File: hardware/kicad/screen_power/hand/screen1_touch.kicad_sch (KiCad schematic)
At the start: 7 parts, among them J101 PI USB / XH4, J102 TOUCH / XH4, K101 IM02TS, Q101 2N7000

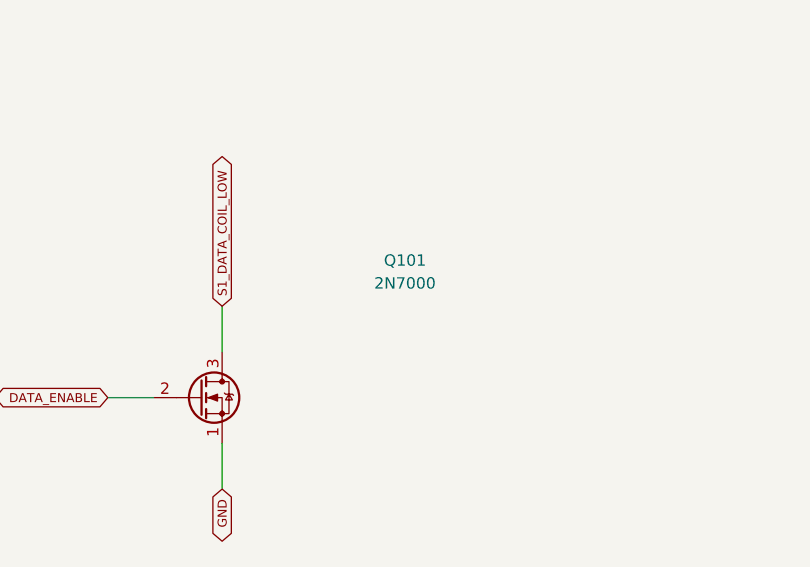
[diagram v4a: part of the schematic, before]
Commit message: fix(hardware): strengthen screen gate drive and finish PCB copper
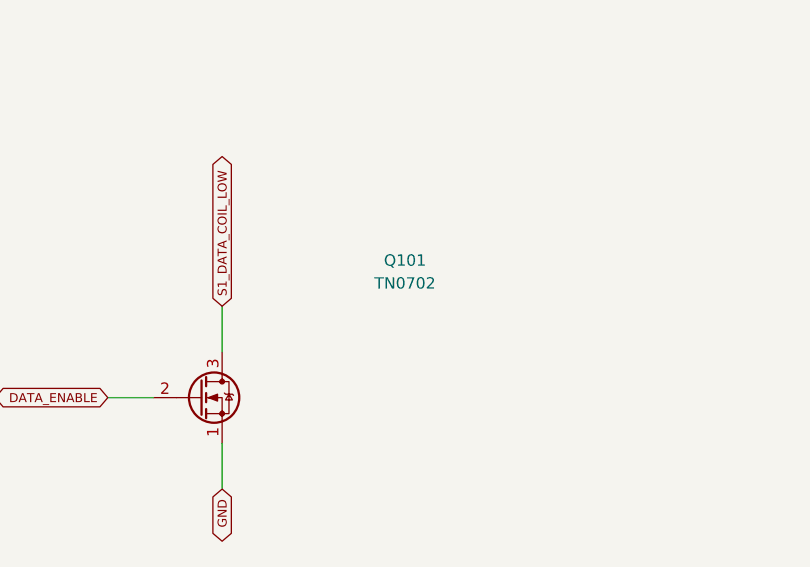
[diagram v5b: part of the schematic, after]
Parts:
- Q101: value 2N7000 -> TN0702; MPN 2N7000 -> TN0702N3-G
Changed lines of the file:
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@@
   (title_block
     (title "Segno screen power / hand / screen1 touch")
-    (rev "K prototype")
+    (rev "L prototype")
     (comment 1 "Discrete 5V switch. Host VBUS powers only its own signal relay coil.")
     (comment 2 "Physical verification required before release."))
@@
         (font
           (size 1.27 1.27))))
-    (property "Value" "2N7000"
+    (property "Value" "TN0702"
       (at 276.86 101.60000000000001 0)
       (effects
@@
           (size 1.27 1.27))
         (hide yes)))
-    (property "MPN" "2N7000"
+    (property "MPN" "TN0702N3-G"
       (at 276.86 114.3 0)
       (effects

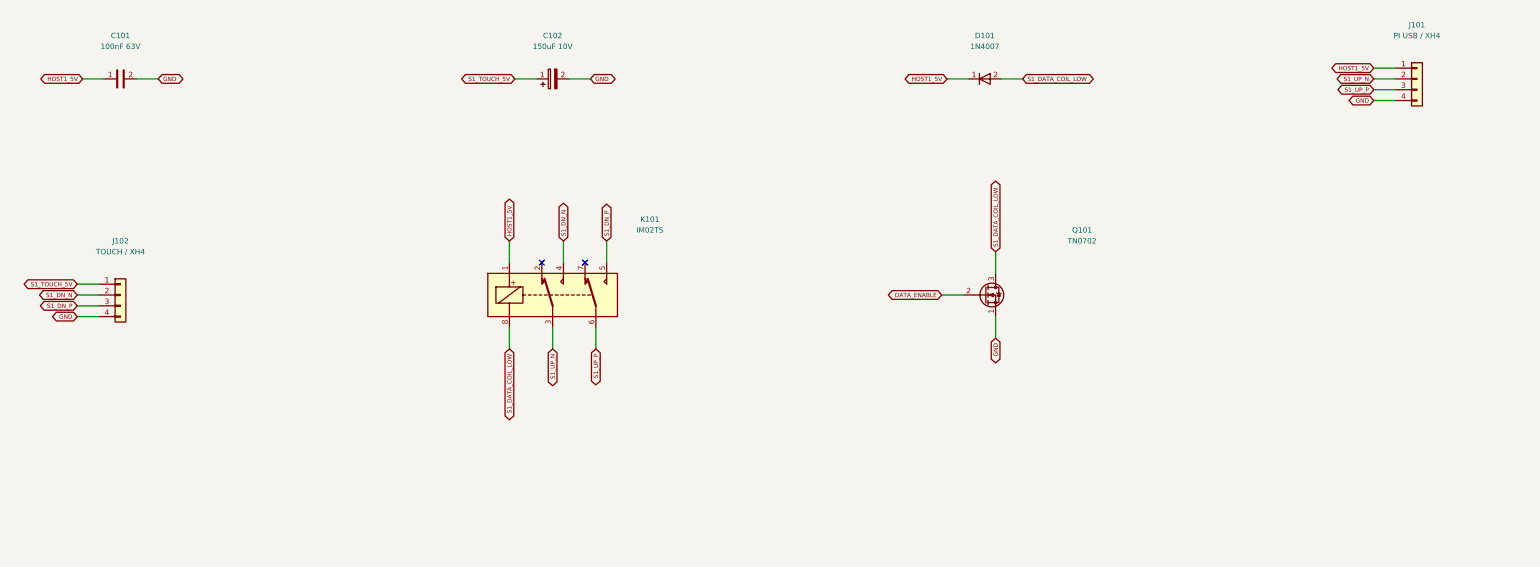
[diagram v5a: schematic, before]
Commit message: fix(hardware): correct USB relay power source and assess revised routing
Prepare Revision M schematic, low-current host sensing and shield drain pads. Keep screen manufacturing on hold pending the revised native layout and complete release validation.
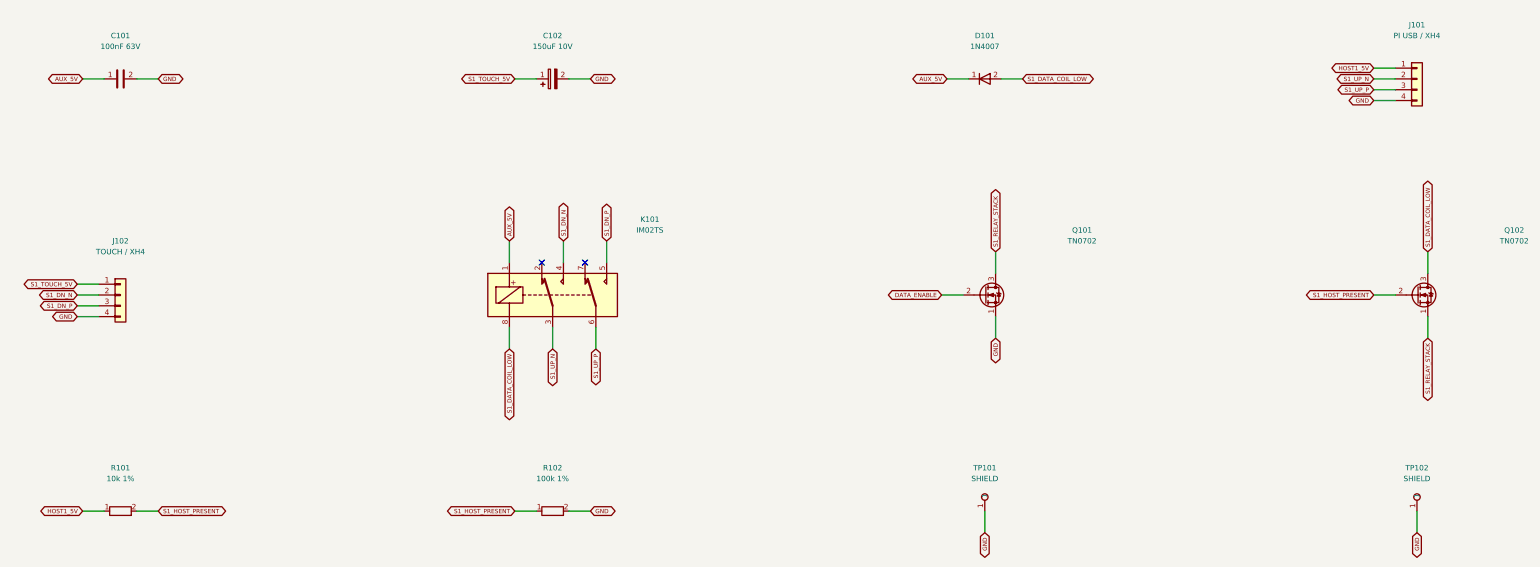
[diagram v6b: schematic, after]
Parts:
- added Q102: TN0702, Package_TO_SOT_THT:TO-92_Inline_Wide, symbol screen_symbols:Transistor_FET_2N7000
- added R101: 10k 1%, Resistor_THT:R_Axial_DIN0207_L6.3mm_D2.5mm_P10.16mm_Horizontal, symbol screen_symbols:Device_R
- added R102: 100k 1%, Resistor_THT:R_Axial_DIN0207_L6.3mm_D2.5mm_P10.16mm_Horizontal, symbol screen_symbols:Device_R
- added TP101, TP102: SHIELD, TestPoint:TestPoint_THTPad_D2.0mm_Drill1.0mm, symbol screen_symbols:Connector_TestPoint
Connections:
- net GND: now also R102.2, TP101.1, TP102.1
- net HOST1_5V: now also R101.1; no longer C101.1, D101.1 (K), K101.1
- net S1_DATA_COIL_LOW: now also Q102.3 (D); no longer Q101.3 (D)
- new net AUX_5V: C101.1, D101.1 (K), K101.1
- new net S1_HOST_PRESENT: Q102.2 (G), R101.2, R102.1
- new net S1_RELAY_STACK: Q101.3 (D), Q102.1 (S)

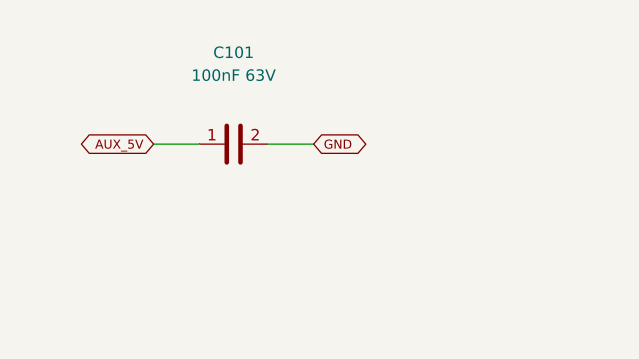
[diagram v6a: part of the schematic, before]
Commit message: feat(hardware): lower screen power cost and finish copper contours
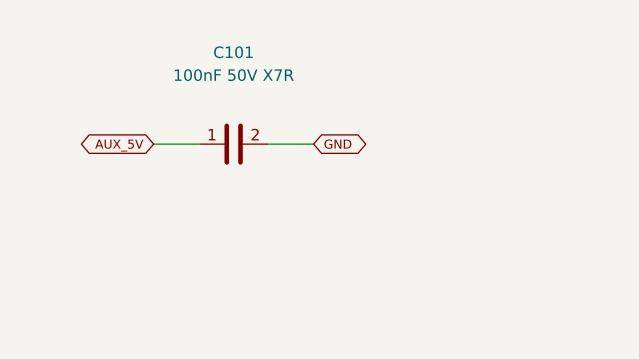
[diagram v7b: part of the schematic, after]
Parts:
- C101: value 100nF 63V -> 100nF 50V X7R; footprint Capacitor_THT:C_Rect_L7.2mm_W2.5mm_P5.00mm -> Capacitor_THT:C_Disc_D7.5mm_W4.4mm_P5.00mm; MPN MKS2C031001A00KSSD -> K104K10X7RF53H5
- D101: MPN 1N4007-E3/54 -> 1N4007G
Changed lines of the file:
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@@
   (title_block
     (title "Segno screen power / hand / screen1 touch")
-    (rev "M prototype")
-    (comment 1 "AUX-powered relays; each host VBUS supplies only its presence detector.")
-    (comment 2 "Physical verification required before release."))
+    (rev "N prototype")
+    (comment 1 "One normally open contact switches AUX; every board load sits behind F1.")
+    (comment 2 "AUX-powered relays; each host VBUS supplies only its presence detector.")
+    (comment 3 "Physical verification required before release."))
   (wire
     (pts
@@
         (font
           (size 1.27 1.27))))
-    (property "Value" "100nF 63V"
+    (property "Value" "100nF 50V X7R"
       (at 50.8 55.88 90)
       (effects
         (font
           (size 1.27 1.27))))
-    (property "Footprint" "Capacitor_THT:C_Rect_L7.2mm_W2.5mm_P5.00mm"
+    (property "Footprint" "Capacitor_THT:C_Disc_D7.5mm_W4.4mm_P5.00mm"
       (at 50.8 63.5 90)
       (effects
@@
           (size 1.27 1.27))
         (hide yes)))
-    (property "MPN" "MKS2C031001A00KSSD"
+    (property "MPN" "K104K10X7RF53H5"
       (at 50.8 63.5 90)
       (effects
@@
           (size 1.27 1.27))
         (hide yes)))
-    (property "MPN" "1N4007-E3/54"
+    (property "MPN" "1N4007G"
       (at 254.0 63.5 0)
       (effects

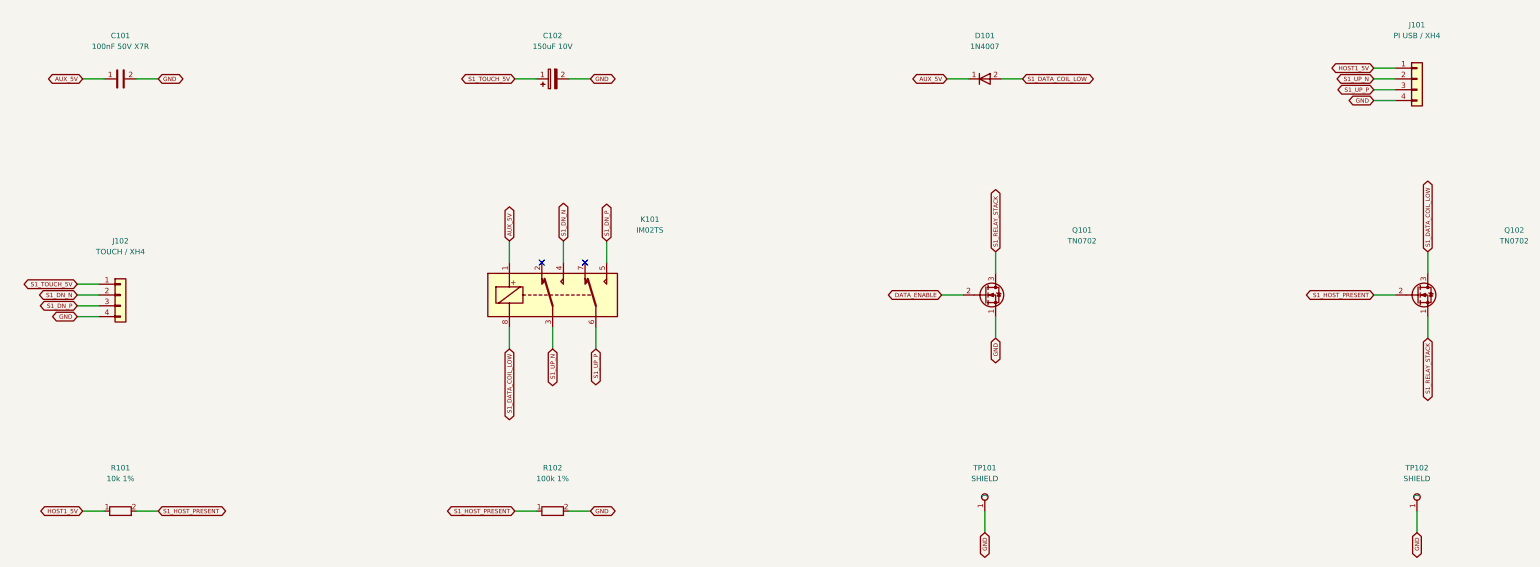
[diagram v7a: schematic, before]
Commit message: feat(hardware): carry USB shields through removable XH5 plugs
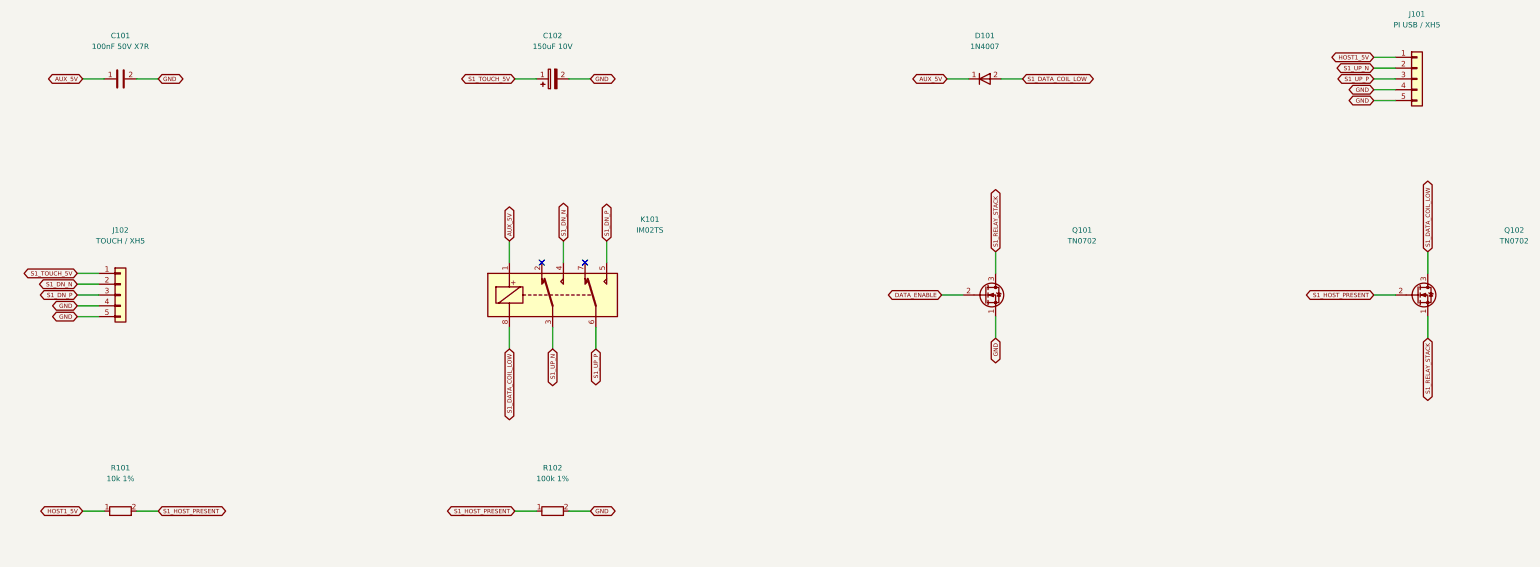
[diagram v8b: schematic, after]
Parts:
- removed TP101, TP102: SHIELD, TestPoint:TestPoint_THTPad_D2.0mm_Drill1.0mm, symbol screen_symbols:Connector_TestPoint
- J101: value PI USB / XH4 -> PI USB / XH5; footprint Connector_JST:JST_XH_B4B-XH-A_1x04_P2.50mm_Vertical -> Connector_JST:JST_XH_B5B-XH-A_1x05_P2.50mm_Vertical; symbol screen_symbols:Connector_Generic_Conn_01x04 -> screen_symbols:Connector_Generic_Conn_01x05; MPN B4B-XH-A(LF)(SN) -> B5B-XH-A(LF)(SN)
- J102: value TOUCH / XH4 -> TOUCH / XH5; footprint Connector_JST:JST_XH_B4B-XH-A_1x04_P2.50mm_Vertical -> Connector_JST:JST_XH_B5B-XH-A_1x05_P2.50mm_Vertical; symbol screen_symbols:Connector_Generic_Conn_01x04 -> screen_symbols:Connector_Generic_Conn_01x05; MPN B4B-XH-A(LF)(SN) -> B5B-XH-A(LF)(SN)
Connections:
- net GND: now also J101.5 (Pin_5), J102.5 (Pin_5)
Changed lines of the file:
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@@
   (title_block
     (title "Segno screen power / hand / screen1 touch")
-    (rev "N prototype")
+    (rev "O prototype")
     (comment 1 "One normally open contact switches AUX; every board load sits behind F1.")
     (comment 2 "AUX-powered relays; each host VBUS supplies only its presence detector.")
@@
   (wire
     (pts
+      (xy 350.52 58.42)
+      (xy 345.44 58.42))
+    (stroke
+      (width 0)
+      (type default))
+)
+  (global_label "HOST1_5V"
+    (shape bidirectional)
+    (at 345.44 58.42 180)
+    (effects
+      (font
+        (size 1.0 1.0))
+      (justify right))
+)
+  (wire
+    (pts
       (xy 350.52 60.96)
       (xy 345.44 60.96))
@@
       (type default))
 )
-  (global_label "HOST1_5V"
+  (global_label "S1_UP_N"
     (shape bidirectional)
     (at 345.44 60.96 180)
@@
       (type default))
 )
-  (global_label "S1_UP_N"
+  (global_label "S1_UP_P"
     (shape bidirectional)
     (at 345.44 63.5 180)
@@
       (type default))
 )
-  (global_label "S1_UP_P"
+  (global_label "GND"
     (shape bidirectional)
     (at 345.44 66.04 180)
@@
 )
   (symbol
-    (lib_id "screen_symbols:Connector_Generic_Conn_01x04")
+    (lib_id "screen_symbols:Connector_Generic_Conn_01x05")
     (at 355.59999999999997 63.5 0)
     (unit 1)
@@
     (dnp no)
     (property "Reference" "J101"
-      (at 355.59999999999997 50.8 0)
-      (effects
-        (font
-          (size 1.27 1.27))))
-    (property "Value" "PI USB / XH4"
-      (at 355.59999999999997 53.339999999999996 0)
-      (effects
-        (font
-          (size 1.27 1.27))))
-    (property "Footprint" "Connector_JST:JST_XH_B4B-XH-A_1x04_P2.50mm_Vertical"
+      (at 355.59999999999997 48.260000000000005 0)
+      (effects
+        (font
+          (size 1.27 1.27))))
+    (property "Value" "PI USB / XH5"
+      (at 355.59999999999997 50.800000000000004 0)
+      (effects
+        (font
+          (size 1.27 1.27))))
+    (property "Footprint" "Connector_JST:JST_XH_B5B-XH-A_1x05_P2.50mm_Vertical"
       (at 355.59999999999997 63.5 0)
       (effects
@@
           (size 1.27 1.27))
         (hide yes)))
-    (property "MPN" "B4B-XH-A(LF)(SN)"
+    (property "MPN" "B5B-XH-A(LF)(SN)"
       (at 355.59999999999997 63.5 0)
       (effects
@@
 )
     (pin "4"
+)
+    (pin "5"
 )
     (instances
@@
   (wire
     (pts
+      (xy 45.72 109.22)
+      (xy 40.64 109.22))
+    (stroke
+      (width 0)
+      (type default))
+)
+  (global_label "S1_TOUCH_5V"
+    (shape bidirectional)
+    (at 40.64 109.22 180)
+    (effects
+      (font
+        (size 1.0 1.0))
+      (justify right))
+)
+  (wire
+    (pts
       (xy 45.72 111.76)
       (xy 40.64 111.76))
@@
       (type default))
 )
-  (global_label "S1_TOUCH_5V"
+  (global_label "S1_DN_N"
     (shape bidirectional)
     (at 40.64 111.76 180)
@@
       (type default))
 )
-  (global_label "S1_DN_N"
+  (global_label "S1_DN_P"
     (shape bidirectional)
     (at 40.64 114.3 180)
@@
       (type default))
 )
-  (global_label "S1_DN_P"
+  (global_label "GND"
     (shape bidirectional)
     (at 40.64 116.84 180)
@@
 )
   (symbol
-    (lib_id "screen_symbols:Connector_Generic_Conn_01x04")
+    (lib_id "screen_symbols:Connector_Generic_Conn_01x05")
     (at 50.8 114.3 0)
     (unit 1)
@@
     (dnp no)
     (property "Reference" "J102"
-      (at 50.8 101.6 0)
-      (effects
-        (font
-          (size 1.27 1.27))))
-    (property "Value" "TOUCH / XH4"
-      (at 50.8 104.14 0)
-      (effects
-        (font
-          (size 1.27 1.27))))
-    (property "Footprint" "Connector_JST:JST_XH_B4B-XH-A_1x04_P2.50mm_Vertical"
+      (at 50.8 99.06 0)
+      (effects
+        (font
+          (size 1.27 1.27))))
+    (property "Value" "TOUCH / XH5"
+      (at 50.8 101.60000000000001 0)
+      (effects
+        (font
+          (size 1.27 1.27))))
+    (property "Footprint" "Connector_JST:JST_XH_B5B-XH-A_1x05_P2.50mm_Vertical"
       (at 50.8 114.3 0)
       (effects
@@
           (size 1.27 1.27))
         (hide yes)))
-    (property "MPN" "B4B-XH-A(LF)(SN)"
+    (property "MPN" "B5B-XH-A(LF)(SN)"
       (at 50.8 114.3 0)
       (effects
@@
 )
     (pin "4"
+)
+    (pin "5"
 )
     (instances
@@
           (reference "R102")
           (unit 1)))))
-  (wire
-    (pts
-      (xy 254.0 165.1)
-      (xy 254.0 170.18))
-    (stroke
-      (width 0)
-      (type default))
-)
-  (global_label "GND"
-    (shape bidirectional)
-    (at 254.0 170.18 270)
-    (effects
-      (font
-        (size 1.0 1.0))
-      (justify right))
-)
-  (symbol
-    (lib_id "screen_symbols:Connector_TestPoint")
-    (at 254.0 165.1 0)
-    (unit 1)
-    (in_bom no)
-    (on_board yes)
-    (dnp no)
-    (property "Reference" "TP101"
-      (at 254.0 154.94 0)
-      (effects
-        (font
-          (size 1.27 1.27))))
-    (property "Value" "SHIELD"
-      (at 254.0 157.48 0)
-      (effects
-        (font
-          (size 1.27 1.27))))
-    (property "Footprint" "TestPoint:TestPoint_THTPad_D2.0mm_Drill1.0mm"
-      (at 254.0 165.1 0)
-      (effects
-        (font
-          (size 1.27 1.27))
-        (hide yes)))
-    (property "MPN" "PCB pad"
-      (at 254.0 165.1 0)
-      (effects
-        (font
-          (size 1.27 1.27))
-        (hide yes)))
-    (pin "1"
-)
-    (instances
-      (project "screen_power_hand"
-        (path "/63a63dd8-c505-5bb8-8418-5eb0e558e546/480ecebe-e95e-539a-a92c-a9448db02fd9"
-          (reference "TP101")
-          (unit 1)))))
-  (wire
-    (pts
-      (xy 355.6 165.1)
-      (xy 355.6 170.18))
-    (stroke
-      (width 0)
-      (type default))
-)
-  (global_label "GND"
-    (shape bidirectional)
-    (at 355.6 170.18 270)
-    (effects
-      (font
-        (size 1.0 1.0))
-      (justify right))
-)
-  (symbol
-    (lib_id "screen_symbols:Connector_TestPoint")
-    (at 355.59999999999997 165.1 0)
-    (unit 1)
-    (in_bom no)
-    (on_board yes)
-    (dnp no)
-    (property "Reference" "TP102"
-      (at 355.59999999999997 154.94 0)
-      (effects
-        (font
-          (size 1.27 1.27))))
-    (property "Value" "SHIELD"
-      (at 355.59999999999997 157.48 0)
-      (effects
-        (font
-          (size 1.27 1.27))))
-    (property "Footprint" "TestPoint:TestPoint_THTPad_D2.0mm_Drill1.0mm"
-      (at 355.59999999999997 165.1 0)
-      (effects
-        (font
-          (size 1.27 1.27))
-        (hide yes)))
-    (property "MPN" "PCB pad"
-      (at 355.59999999999997 165.1 0)
-      (effects
-        (font
-          (size 1.27 1.27))
-        (hide yes)))
-    (pin "1"
-)
-    (instances
-      (project "screen_power_hand"
-        (path "/63a63dd8-c505-5bb8-8418-5eb0e558e546/480ecebe-e95e-539a-a92c-a9448db02fd9"
-          (reference "TP102")
-          (unit 1)))))
   (embedded_fonts no))
